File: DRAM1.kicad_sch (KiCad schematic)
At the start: 8 parts, among them IC112 TMM41256AP, IC113 TMM41256AP, IC114 TMM41256AP, IC115 TMM41256AP, IC116 TMM41256AP, IC117 TMM41256AP, IC118 TMM41256AP, IC119 TMM41256AP

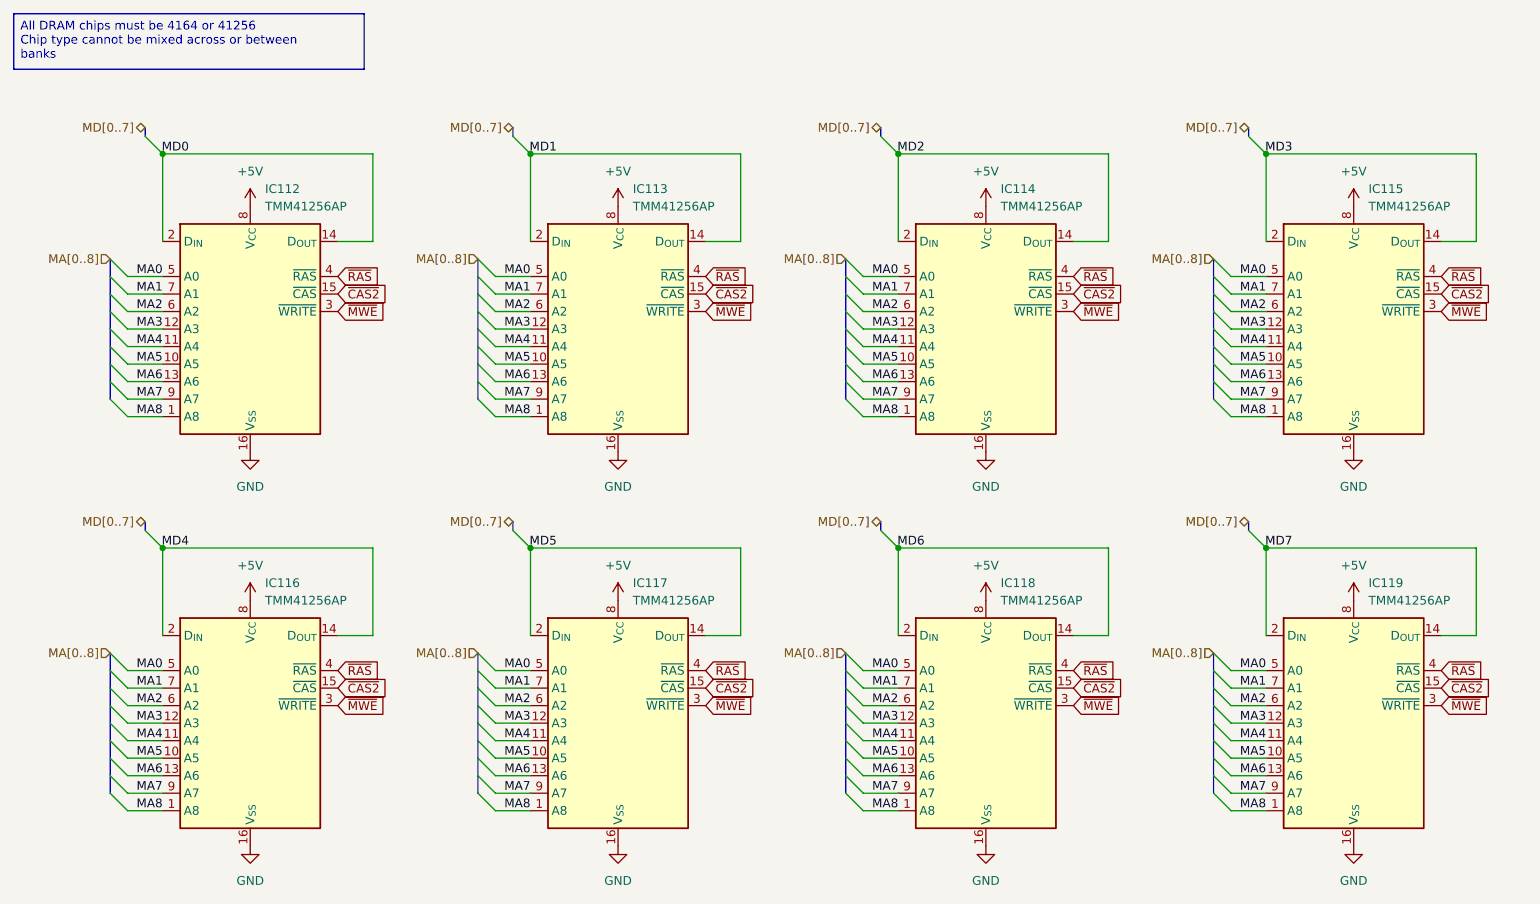
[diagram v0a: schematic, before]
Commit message: fix incorrect gate array pin numbering
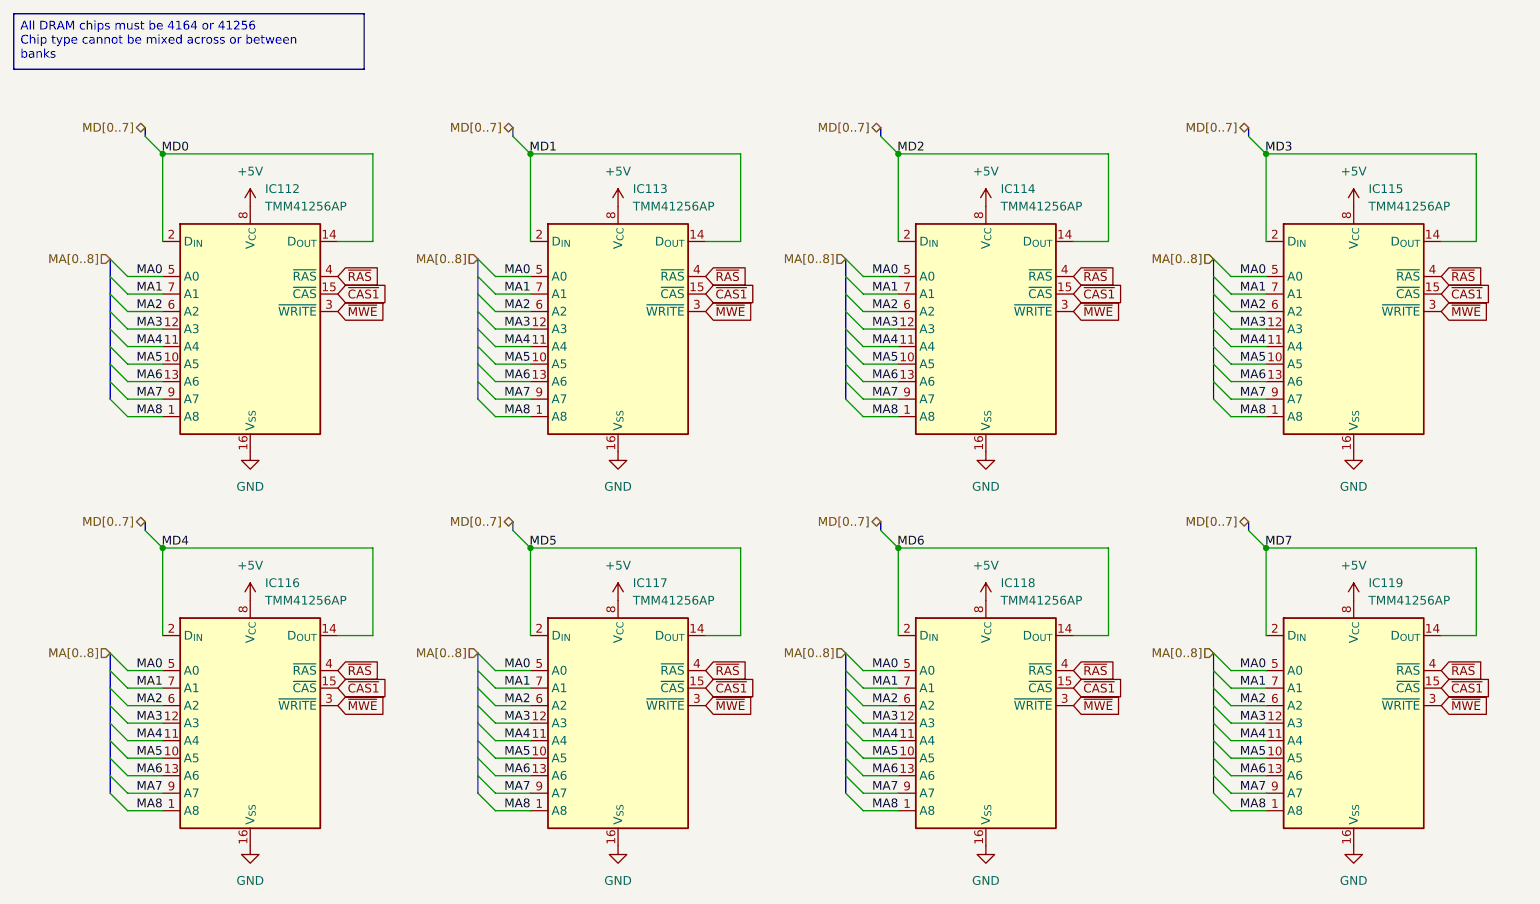
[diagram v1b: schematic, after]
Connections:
- net ~{CAS2} renamed ~{CAS1}
